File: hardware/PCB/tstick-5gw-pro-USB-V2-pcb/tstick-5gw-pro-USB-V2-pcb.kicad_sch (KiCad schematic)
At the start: 68 parts, among them J1 USB_C_Receptacle_USB2.0, Q1 BSS138, Q2 BSS138, Q3 BSS138, SW1 B3U-1000P, SW2 B3U-1000P, U1 USBLC6-2P6, U2 MCP73871, U3 NCP167AMX330TBG, U4 NCP167AMX180TBG

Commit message: bumped up all package sizes from a minimum of 0201 to 0402
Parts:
- added C13: 10uF, Capacitor_SMD:C_0603_1608Metric, symbol Device:C
- added C19: 0.1uF, Capacitor_SMD:C_0402_1005Metric, symbol Device:C
- added SYS2: SYS, symbol power-symbols:VSYS
- BT1, BT2: footprint Connector_JST:JST_PH_B2B-PH-SM4-TB_1x02-1MP_P2.00mm_Vertical -> Connector_JST:JST_PH_S2B-PH-SM4-TB_1x02-1MP_P2.00mm_Horizontal; Description Value Pkg Connector Header Surface Mount 2 position 0.079" (2.00mm) -> Connector Header Surface Mount, Right Angle 2 position 0.07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; Mfg Part # B2B-PH-SM4-TB -> S2B-PH-SM4-TB
- C1, C15, C6, C7: footprint Capacitor_SMD:C_0201_0603Metric -> Capacitor_SMD:C_0402_1005Metric; Description Value Pkg 0.1 µF ±10% 10V Ceramic Capacitor X5R 0201 (0603 Metric) -> 0.1 µF ±10% 16V Ceramic Capacitor X7R 0402 (1005 Metric); Mfg Part # CL03A104KP3NNNC -> CL05B104KO5NNNC; mpn CL03A104KP3NNNC -> CL05B104KO5NNNC
- C10, C11, C12, C4, C5, C9: footprint Capacitor_SMD:C_0201_0603Metric -> Capacitor_SMD:C_0402_1005Metric; Description Value Pkg 1 µF ±10% 6.3V Ceramic Capacitor X5R 0201 (0603 Metric) -> 1 µF ±10% 16V Ceramic Capacitor X5R 0402 (1005 Metric); Mfg Part # CL03A105KQ3CSNC -> CL05A105KO5NNNC; mpn CL03A105KQ3CSNC -> CL05A105KO5NNNC
- C14: Mfg Part # CL10A106KQ8NNNC -> CL10A105KO8NNNC; mpn CL10A106KQ8NNNC -> CL10A105KO8NNNC
- C2: footprint Capacitor_SMD:C_0201_0603Metric -> Capacitor_SMD:C_0402_1005Metric; Description Value Pkg 0.47 µF ±10% 6.3V Ceramic Capacitor X5R 0201 (0603 Metric) -> 0.47 µF ±10% 16V Ceramic Capacitor X5R 0402 (1005 Metric); Manufacturer Samsung Electro-Mechanics -> Murata Electronics; Mfg Part # CL03A474KQ3NNNC -> GRT155R61C474KE01D; mpn CL03A474KQ3NNNC -> GRT155R61C474KE01D
- C3, C8: footprint Capacitor_SMD:C_0201_0603Metric -> Capacitor_SMD:C_0603_1608Metric; Description Value Pkg 4.7 µF ±20% 6.3V Ceramic Capacitor X5R 0201 (0603 Metric) -> 4.7 µF ±10% 16V Ceramic Capacitor X5R 0603 (1608 Metric); Mfg Part # CL03A475MQ5C65C -> CL10A475KO8NNNC; mpn CL03A475MQ5C65C -> CL10A475KO8NNNC
- R1, R10, R22, R24, R3, R8: footprint Resistor_SMD:R_0201_0603Metric -> Resistor_SMD:R_0402_1005Metric; Description Value Pkg 1 kOhms ±1% 0.05W, 1/20W Chip Resistor 0201 (0603 Metric) T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 -> 1 kOhms ±1% 0.1W, 1/10W Chip Resistor 0402 (1005 Metric) Au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; Mfg Part # ERJ-1GNF1001C -> ERJ-2RKF1001X; mpn ERJ-1GNF1001C -> ERJ-2RKF1001X
- R12, R5: footprint Resistor_SMD:R_0201_0603Metric -> Resistor_SMD:R_0402_1005Metric; Description Value Pkg 10 kOhms ±1% 0.05W, 1/20W Chip Resistor 0201 (0603 Metric) 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 -> 10 kOhms ±1% 0.1W, 1/10W Chip Resistor 0402 (1005 Metric) A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; Mfg Part # ERJ-1GNF1002C -> ERJ-2RKF1002X; mpn ERJ-1GNF1002C -> ERJ-2RKF1002X
- R14, R15, R16, R19, R21, R23: footprint Resistor_SMD:R_0201_0603Metric -> Resistor_SMD:R_0402_1005Metric; Description Value Pkg 2.2 kOhms ±1% 0.05W, 1/20W Chip Resistor 0201 (0603 Metric)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 -> 2.2 kOhms ±1% 0.1W, 1/10W Chip Resistor 0402 (1005 Metric) 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; Mfg Part # ERJ-1GNF2201C -> ERJ-2RKF2201X; mpn ERJ-1GNF2201C -> ERJ-2RKF2201X
- R17: footprint Resistor_SMD:R_0201_0603Metric -> Resistor_SMD:R_0402_1005Metric; Description Value Pkg 24.9 kOhms ±1% 0.05W, 1/20W Chip Resistor 0201 (0603 Metric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 -> 24.9 kOhms ±1% 0.1W, 1/10W Chip Resistor 0402 (1005 Metric)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; Mfg Part # ERJ-1GNF2492C -> ERJ-2RKF2492X; mpn ERJ-1GNF2492C -> ERJ-2RKF2492X
- R18: footprint Resistor_SMD:R_0201_0603Metric -> Resistor_SMD:R_0402_1005Metric; Description Value Pkg 330 kOhms ±1% 0.05W, 1/20W Chip Resistor 0201 (0603 Metric)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 -> 330 kOhms ±1% 0.1W, 1/10W Chip Resistor 0402 (1005 Metric) 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; Mfg Part # ERJ-1GNF3303C -> ERJ-2RKF3303X; mpn ERJ-1GNF3303C -> ERJ-2RKF3303X
- R20: footprint Resistor_SMD:R_0201_0603Metric -> Resistor_SMD:R_0402_1005Metric; Description Value Pkg 2 kOhms ±1% 0.05W, 1/20W Chip Resistor 0201 (0603 Metric) T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 -> 2 kOhms ±1% 0.1W, 1/10W Chip Resistor 0402 (1005 Metric) Au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; Mfg Part # ERJ-1GNF2001C -> ERJ-2RKF2001X; mpn ERJ-1GNF2001C -> ERJ-2RKF2001X
- R4: footprint Resistor_SMD:R_0201_0603Metric -> Resistor_SMD:R_0402_1005Metric; Description Value Pkg 110 kOhms ±1% 0.05W, 1/20W Chip Resistor 0201 (0603 Metric)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 -> 110 kOhms ±1% 0.1W, 1/10W Chip Resistor 0402 (1005 Metric) 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; Mfg Part # ERJ-1GNF1103C -> ERJ-2RKF1103X; mpn ERJ-1GNF1103C -> ERJ-2RKF1103X
- R6, R7: footprint Resistor_SMD:R_0201_0603Metric -> Resistor_SMD:R_0402_1005Metric; Description Value Pkg 5.1 kOhms ±5% 0.05W, 1/20W Chip Resistor 0201 (0603 Metric)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 -> 5.1 kOhms ±1% 0.1W, 1/10W Chip Resistor 0402 (1005 Metric) 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; Mfg Part # ERJ-1GNJ512C -> ERJ-2RKF5101X; mpn ERJ-1GNJ512C -> ERJ-2RKF5101X
- R9: footprint Resistor_SMD:R_0201_0603Metric -> Resistor_SMD:R_0402_1005Metric; Description Value Pkg 10 kOhms ±1% 0.05W, 1/20W Chip Resistor 0201 (0603 Metric) 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 -> 10 kOhms ±1% 0.1W, 1/10W Chip Resistor 0402 (1005 Metric) A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; Mfg Part # ERJ-1GNF1002C -> ERJ-2RKF1002X; mpn ERJ-1GNF2492C -> ERJ-2RKF1002X
- TH1: footprint Resistor_SMD:R_0201_0603Metric -> Resistor_SMD:R_0402_1005Metric; Description Value Pkg NTC Thermistor 10k 0201 (0603 Metric) -> NTC Thermistor 10k 0402 (1005 Metric); Mfg Part # ERT-JZEG103FA -> ERT-J0EG103FA
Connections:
- net +3V3: now also BOARDLAYOUT1.17 (3v3), BOARDLAYOUT1.5 (SYS), C13.1, C19.1; no longer BOARDLAYOUT1.21 (3v3), BOARDLAYOUT1.3 (3v3)
- net CIPO: now also BOARDLAYOUT1.13 (CIPO); no longer BOARDLAYOUT1.17 (CIPO)
- net COPI: now also BOARDLAYOUT1.11 (COPI); no longer BOARDLAYOUT1.15 (COPI)
- net EN: now also BOARDLAYOUT1.6 (EN); no longer BOARDLAYOUT1.9 (EN)
- net GND: now also BOARDLAYOUT1.16 (GND), BOARDLAYOUT1.7 (GND), C13.2, C19.2; no longer BOARDLAYOUT1.10 (GND), BOARDLAYOUT1.20 (GND)
- net IO1: now also BOARDLAYOUT1.8 (IO01); no longer BOARDLAYOUT1.11 (IO01)
- net IO18: no longer BOARDLAYOUT1.6 (EXTLED)
- net IO2: now also BOARDLAYOUT1.9 (IO02); no longer BOARDLAYOUT1.12 (IO02)
- net IO4: no longer BOARDLAYOUT1.13 (IO04)
- net IO5: no longer BOARDLAYOUT1.14 (IO05)
- net IO6: no longer BOARDLAYOUT1.8 (IO06)
- net IO7: no longer BOARDLAYOUT1.7 (IO07)
- net IO8: now also BOARDLAYOUT1.10 (IO08); no longer BOARDLAYOUT1.5 (IO08)
- net SCK: now also BOARDLAYOUT1.12 (SCK); no longer BOARDLAYOUT1.16 (SCK)
- net SCL: now also BOARDLAYOUT1.15 (SCL); no longer BOARDLAYOUT1.19 (SCL)
- net SDA: now also BOARDLAYOUT1.14 (SDA); no longer BOARDLAYOUT1.18 (SDA)
- net SYS: now also BOARDLAYOUT1.3 (3v3), SYS2.1 (SYS)
- net VUSB: now also BOARDLAYOUT1.18 (5v); no longer BOARDLAYOUT1.22 (5v)

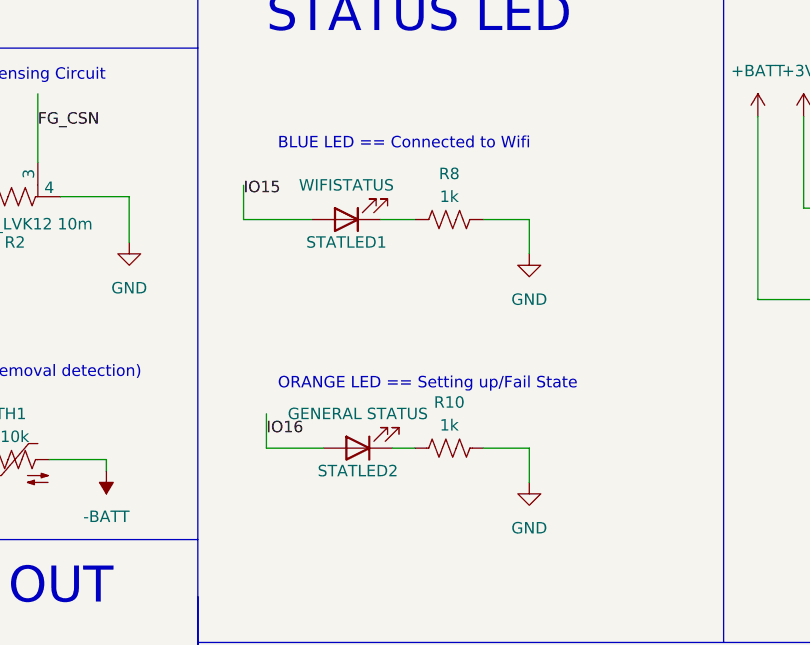
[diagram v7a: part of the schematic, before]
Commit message: moved LEDs, to the front of the board, took new screenshots
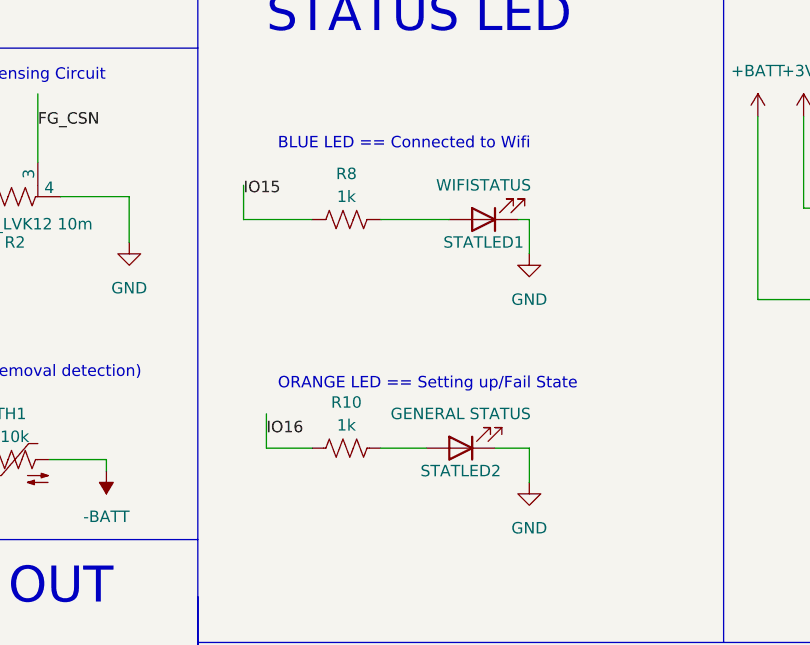
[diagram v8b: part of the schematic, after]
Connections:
- net GND: now also STATLED1.1 (K), STATLED2.1 (K); no longer R10.2, R8.2
- net IO15: now also R8.1; no longer STATLED1.2 (A)
- net IO16: now also R10.1; no longer STATLED2.2 (A)
- new net: R8.2, STATLED1.2 (A)
- new net: R10.2, STATLED2.2 (A)
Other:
- moved on the sheet: R10, R8, STATLED1, STATLED2
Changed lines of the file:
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@@
     (stroke (width 0) (type default))
   )
-  (wire (pts (xy 281.94 165.1) (xy 288.29 165.1))
+  (wire (pts (xy 294.64 165.1) (xy 299.72 165.1))
     (stroke (width 0) (type default))
   )
@@
     (stroke (width 0) (type default))
   )
-  (wire (pts (xy 311.15 139.7) (xy 306.07 139.7))
-    (stroke (width 0) (type default))
-  )
   (wire (pts (xy 55.88 87.63) (xy 55.88 82.55))
     (stroke (width 0) (type default))
@@
     (stroke (width 0) (type default))
   )
+  (wire (pts (xy 307.34 165.1) (xy 311.15 165.1))
+    (stroke (width 0) (type default))
+  )
   (wire (pts (xy 157.48 205.74) (xy 163.83 205.74))
     (stroke (width 0) (type default))
@@
     (stroke (width 0) (type default))
   )
-  (wire (pts (xy 294.64 139.7) (xy 298.45 139.7))
-    (stroke (width 0) (type default))
-  )
   (wire (pts (xy 30.48 129.54) (xy 38.1 129.54))
     (stroke (width 0) (type default))
   )
-  (wire (pts (xy 311.15 165.1) (xy 306.07 165.1))
-    (stroke (width 0) (type default))
-  )
   (wire (pts (xy 132.08 43.18) (xy 132.08 48.26))
     (stroke (width 0) (type default))
@@
     (stroke (width 0) (type default))
   )
+  (wire (pts (xy 294.64 139.7) (xy 302.26 139.7))
+    (stroke (width 0) (type default))
+  )
   (wire (pts (xy 31.75 69.85) (xy 38.1 69.85))
     (stroke (width 0) (type default))
@@
     (stroke (width 0) (type default))
   )
+  (wire (pts (xy 309.88 139.7) (xy 311.15 139.7))
+    (stroke (width 0) (type default))
+  )
   (wire (pts (xy 363.22 67.31) (xy 363.22 69.85))
     (stroke (width 0) (type default))
@@
     (stroke (width 0) (type default))
   )
-  (wire (pts (xy 295.91 165.1) (xy 298.45 165.1))
-    (stroke (width 0) (type default))
-  )
   (wire (pts (xy 226.06 207.01) (xy 226.06 217.17))
     (stroke (width 0) (type default))
@@
     (stroke (width 0) (type default))
   )
+  (wire (pts (xy 281.94 165.1) (xy 287.02 165.1))
+    (stroke (width 0) (type default))
+  )
   (wire (pts (xy 35.56 264.16) (xy 34.29 264.16))
     (stroke (width 0) (type default))
@@
     (effects (font (size 1.27 1.27)) (justify left bottom))
   )
-  (symbol (lib_id "Device:R_US") (at 302.26 139.7 90) (unit 1)
+  (symbol (lib_id "Device:R_US") (at 290.83 139.7 90) (unit 1)
     (in_bom yes) (on_board yes) (dnp no)
-    (property "Reference" "R8" (at 302.26 134.62 90)
+    (property "Reference" "R8" (at 290.83 134.62 90)
       (effects (font (size 1.27 1.27)))
     )
-    (property "Value" "1k" (at 302.26 137.16 90)
+    (property "Value" "1k" (at 290.83 137.16 90)
       (effects (font (size 1.27 1.27)))
     )
-    (property "Footprint" "Resistor_SMD:R_0402_1005Metric" (at 302.514 138.684 90)
+    (property "Footprint" "Resistor_SMD:R_0402_1005Metric" (at 291.084 138.684 90)
       (effects (font (size 1.27 1.27)) hide)
     )
-    (property "Datasheet" "https://industrial.panasonic.com/cdbs/www-data/pdf/RDA0000/AOA0000C304.pdf" (at 302.26 139.7 0)
+    (property "Datasheet" "https://industrial.panasonic.com/cdbs/www-data/pdf/RDA0000/AOA0000C304.pdf" (at 290.83 139.7 0)
       (effects (font (size 1.27 1.27)) hide)
     )
-    (property "Description Value Pkg" "1 kOhms ±1% 0.1W, 1/10W Chip Resistor 0402 (1005 Metric) Automotive AEC-Q200 Thick Film" (at 302.26 139.7 0)
+    (property "Description Value Pkg" "1 kOhms ±1% 0.1W, 1/10W Chip Resistor 0402 (1005 Metric) Automotive AEC-Q200 Thick Film" (at 290.83 139.7 0)
       (effects (font (size 1.27 1.27)) hide)
     )
-    (property "Mfg Part #" "ERJ-2RKF1001X" (at 302.26 139.7 0)
+    (property "Mfg Part #" "ERJ-2RKF1001X" (at 290.83 139.7 0)
       (effects (font (size 1.27 1.27)) hide)
     )
-    (property "Manufacturer" "Panasonic Electronic Components" (at 302.26 139.7 0)
+    (property "Manufacturer" "Panasonic Electronic Components" (at 290.83 139.7 0)
       (effects (font (size 1.27 1.27)) hide)
     )
-    (property "mpn" "ERJ-2RKF1001X" (at 302.26 139.7 0)
+    (property "mpn" "ERJ-2RKF1001X" (at 290.83 139.7 0)
       (effects (font (size 1.27 1.27)) hide)
     )
@@
     )
   )
-  (symbol (lib_id "Device:R_US") (at 302.26 165.1 90) (unit 1)
+  (symbol (lib_id "Device:R_US") (at 290.83 165.1 90) (unit 1)
     (in_bom yes) (on_board yes) (dnp no)
-    (property "Reference" "R10" (at 302.26 160.02 90)
+    (property "Reference" "R10" (at 290.83 160.02 90)
       (effects (font (size 1.27 1.27)))
     )
-    (property "Value" "1k" (at 302.26 162.56 90)
+    (property "Value" "1k" (at 290.83 162.56 90)
       (effects (font (size 1.27 1.27)))
     )
-    (property "Footprint" "Resistor_SMD:R_0402_1005Metric" (at 302.514 164.084 90)
+    (property "Footprint" "Resistor_SMD:R_0402_1005Metric" (at 291.084 164.084 90)
       (effects (font (size 1.27 1.27)) hide)
     )
-    (property "Datasheet" "https://industrial.panasonic.com/cdbs/www-data/pdf/RDA0000/AOA0000C304.pdf" (at 302.26 165.1 0)
+    (property "Datasheet" "https://industrial.panasonic.com/cdbs/www-data/pdf/RDA0000/AOA0000C304.pdf" (at 290.83 165.1 0)
       (effects (font (size 1.27 1.27)) hide)
     )
-    (property "Description Value Pkg" "1 kOhms ±1% 0.1W, 1/10W Chip Resistor 0402 (1005 Metric) Automotive AEC-Q200 Thick Film" (at 302.26 165.1 0)
+    (property "Description Value Pkg" "1 kOhms ±1% 0.1W, 1/10W Chip Resistor 0402 (1005 Metric) Automotive AEC-Q200 Thick Film" (at 290.83 165.1 0)
       (effects (font (size 1.27 1.27)) hide)
     )
-    (property "Mfg Part #" "ERJ-2RKF1001X" (at 302.26 165.1 0)
+    (property "Mfg Part #" "ERJ-2RKF1001X" (at 290.83 165.1 0)
       (effects (font (size 1.27 1.27)) hide)
     )
-    (property "Manufacturer" "Panasonic Electronic Components" (at 302.26 165.1 0)
+    (property "Manufacturer" "Panasonic Electronic Components" (at 290.83 165.1 0)
       (effects (font (size 1.27 1.27)) hide)
     )
-    (property "mpn" "ERJ-2RKF1001X" (at 302.26 165.1 0)
+    (property "mpn" "ERJ-2RKF1001X" (at 290.83 165.1 0)
       (effects (font (size 1.27 1.27)) hide)
     )
@@
     )
   )
-  (symbol (lib_id "Device:LED") (at 292.1 165.1 180) (unit 1)
+  (symbol (lib_id "Device:LED") (at 303.53 165.1 180) (unit 1)
     (in_bom yes) (on_board yes) (dnp no)
-    (property "Reference" "STATLED2" (at 292.1 167.64 0)
+    (property "Reference" "STATLED2" (at 303.53 167.64 0)
       (effects (font (size 1.27 1.27)))
     )
-    (property "Value" "GENERAL STATUS" (at 292.1 161.29 0)
+    (property "Value" "GENERAL STATUS" (at 303.53 161.29 0)
       (effects (font (size 1.27 1.27)))
     )
-    (property "Footprint" "LED_SMD:LED_0402_1005Metric" (at 292.1 165.1 0)
+    (property "Footprint" "LED_SMD:LED_0402_1005Metric" (at 303.53 165.1 0)
       (effects (font (size 1.27 1.27)) hide)
     )
-    (property "Datasheet" "https://www.kingbrightusa.com/images/catalog/SPEC/APHHS1005SURCK.pdf" (at 292.1 165.1 0)
+    (property "Datasheet" "https://www.kingbrightusa.com/images/catalog/SPEC/APHHS1005SURCK.pdf" (at 303.53 165.1 0)
       (effects (font (size 1.27 1.27)) hide)
     )
-    (property "Description Value Pkg" "Orange 601nm LED Indication - Discrete 2.1V 0402 (1005 Metric)" (at 292.1 165.1 0)
+    (property "Description Value Pkg" "Orange 601nm LED Indication - Discrete 2.1V 0402 (1005 Metric)" (at 303.53 165.1 0)
       (effects (font (size 1.27 1.27)) hide)
     )
-    (property "Mfg Part #" "APHHS1005SECK" (at 292.1 165.1 0)
+    (property "Mfg Part #" "APHHS1005SECK" (at 303.53 165.1 0)
       (effects (font (size 1.27 1.27)) hide)
     )
-    (property "Manufacturer" "Kingbright" (at 292.1 165.1 0)
+    (property "Manufacturer" "Kingbright" (at 303.53 165.1 0)
       (effects (font (size 1.27 1.27)) hide)
     )
-    (property "mpn" "APHHS1005SURCK" (at 292.1 165.1 0)
+    (property "mpn" "APHHS1005SURCK" (at 303.53 165.1 0)
       (effects (font (size 1.27 1.27)) hide)
     )
@@
     )
   )
-  (symbol (lib_id "Device:LED") (at 290.83 139.7 180) (unit 1)
+  (symbol (lib_id "Device:LED") (at 306.07 139.7 180) (unit 1)
     (in_bom yes) (on_board yes) (dnp no)
-    (property "Reference" "STATLED1" (at 290.83 142.24 0)
+    (property "Reference" "STATLED1" (at 306.07 142.24 0)
       (effects (font (size 1.27 1.27)))
     )
-    (property "Value" "WIFISTATUS" (at 290.83 135.89 0)
+    (property "Value" "WIFISTATUS" (at 306.07 135.89 0)
       (effects (font (size 1.27 1.27)))
     )
-    (property "Footprint" "LED_SMD:LED_0402_1005Metric" (at 290.83 139.7 0)
+    (property "Footprint" "LED_SMD:LED_0402_1005Metric" (at 306.07 139.7 0)
       (effects (font (size 1.27 1.27)) hide)
     )
-    (property "Datasheet" "https://www.kingbrightusa.com/images/catalog/SPEC/APHHS1005SURCK.pdf" (at 290.83 139.7 0)
+    (property "Datasheet" "https://www.kingbrightusa.com/images/catalog/SPEC/APHHS1005SURCK.pdf" (at 306.07 139.7 0)
       (effects (font (size 1.27 1.27)) hide)
     )
-    (property "Description Value Pkg" "Blue 465nm LED Indication - Discrete 3.3V 0402 (1005 Metric)" (at 290.83 139.7 0)
+    (property "Description Value Pkg" "Blue 465nm LED Indication - Discrete 3.3V 0402 (1005 Metric)" (at 306.07 139.7 0)
       (effects (font (size 1.27 1.27)) hide)
     )
-    (property "Mfg Part #" "APHHS1005QBC/D" (at 290.83 139.7 0)
+    (property "Mfg Part #" "APHHS1005QBC/D" (at 306.07 139.7 0)
       (effects (font (size 1.27 1.27)) hide)
     )
-    (property "Manufacturer" "Kingbright" (at 290.83 139.7 0)
+    (property "Manufacturer" "Kingbright" (at 306.07 139.7 0)
       (effects (font (size 1.27 1.27)) hide)
     )
-    (property "mpn" "APHHS1005SURCK" (at 290.83 139.7 0)
+    (property "mpn" "APHHS1005SURCK" (at 306.07 139.7 0)
       (effects (font (size 1.27 1.27)) hide)
     )
